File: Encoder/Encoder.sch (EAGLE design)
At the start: 4 parts, among them IC1 4017D

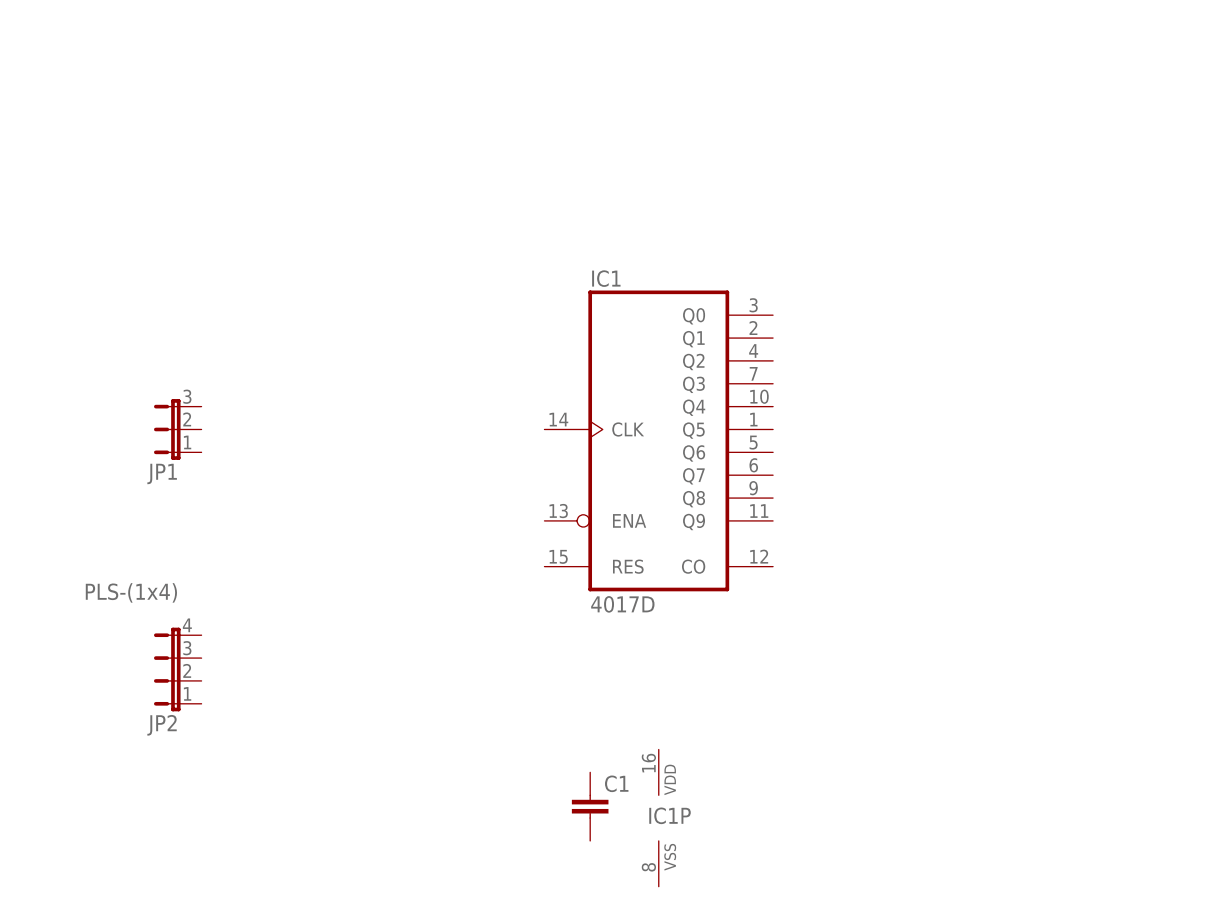
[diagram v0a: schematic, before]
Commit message: Added a pcb for encoder: made scheme, library and prearranged components on the board
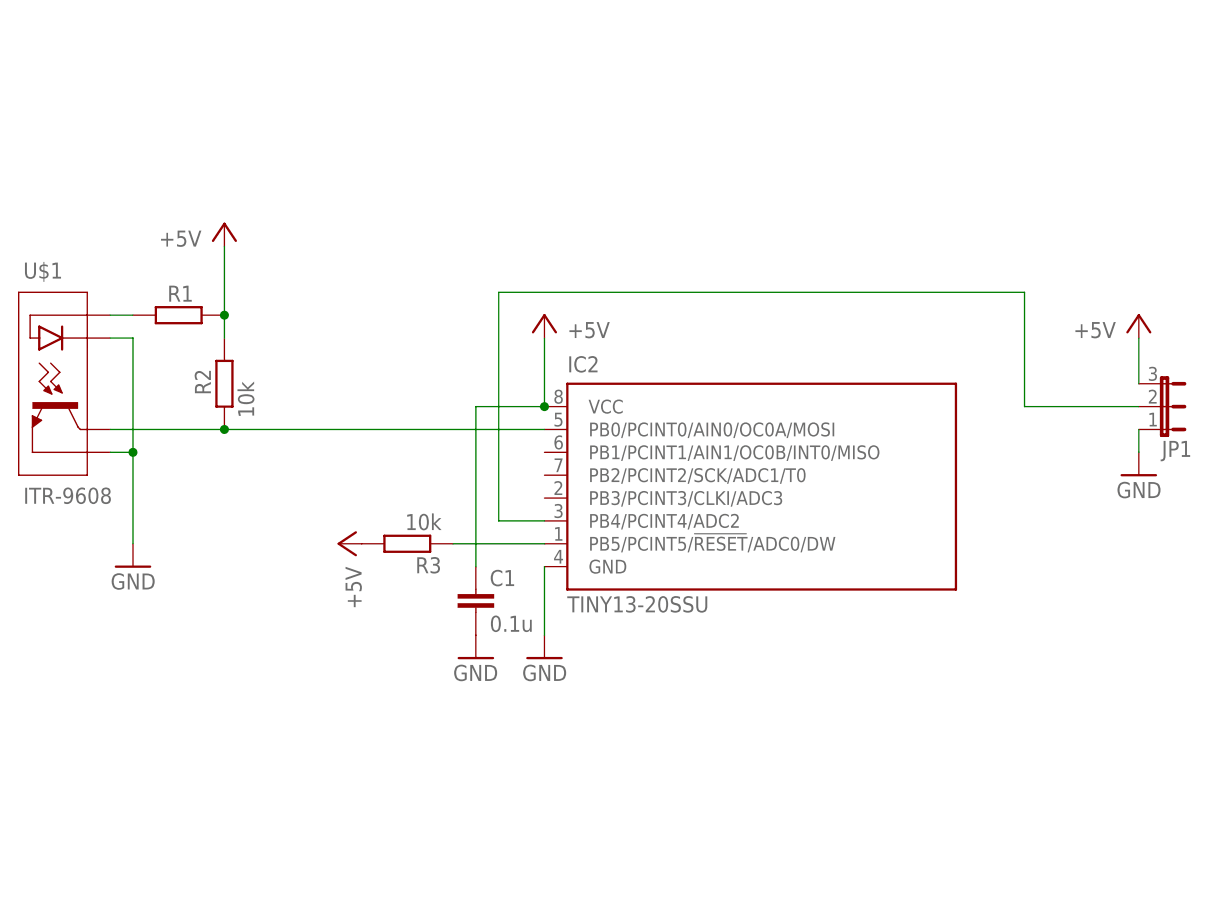
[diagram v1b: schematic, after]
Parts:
- removed IC1: 4017D, 40xx:4017D
- removed JP2: PLS-(1х4), jumper:PLS-(1х4)
- added IC2: TINY13-20SSU, atmel:TINY13-20SSU
- added R1: (no value), rcl:R-EU_M0805
- added R2, R3: 10k, rcl:R-EU_M0805
- added U$1: ITR-9608, EncoderLib:ITR-9608
- C1: value (none) -> 0.1u
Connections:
- new net !RES: IC2.PB5/PCINT5/!RESET!/ADC0/DW, R3.1
- new net +5V: C1.1, IC2.VCC, JP1.3, R1.2, R2.2, R3.2
- new net DATA-IN: IC2.PB0/PCINT0/AIN0/OC0A/MOSI, R2.1, U$1.C
- new net DATA-OUT: IC2.PB4/PCINT4/ADC2, JP1.2
- new net GND: C1.2, IC2.GND, JP1.1, U$1.E, U$1.K
- new net N$2: R1.1, U$1.A
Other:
- moved on the sheet: C1, JP1
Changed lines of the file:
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@@
 </classes>
 <parts>
-<part name="IC1" library="40xx" library_urn="urn:adsk.eagle:library:80" deviceset="4017" device="D" package3d_urn="urn:adsk.eagle:package:821/2"/>
-<part name="C1" library="rcl" library_urn="urn:adsk.eagle:library:334" deviceset="C-EU" device="C0805" package3d_urn="urn:adsk.eagle:package:23617/2"/>
+<part name="C1" library="rcl" library_urn="urn:adsk.eagle:library:334" deviceset="C-EU" device="C0805" package3d_urn="urn:adsk.eagle:package:23617/2" value="0.1u"/>
 <part name="JP1" library="jumper" library_urn="urn:adsk.eagle:library:252" deviceset="JP2E" device="" package3d_urn="urn:adsk.eagle:package:15452/1"/>
-<part name="JP2" library="jumper" deviceset="PLS-(1х4)" device=""/>
+<part name="R1" library="rcl" library_urn="urn:adsk.eagle:library:334" deviceset="R-EU_" device="M0805" package3d_urn="urn:adsk.eagle:package:23556/2"/>
+<part name="P+1" library="supply1" library_urn="urn:adsk.eagle:library:371" deviceset="+5V" device=""/>
+<part name="GND1" library="supply1" library_urn="urn:adsk.eagle:library:371" deviceset="GND" device=""/>
+<part name="P+2" library="supply1" library_urn="urn:adsk.eagle:library:371" deviceset="+5V" device=""/>
+<part name="GND2" library="supply1" library_urn="urn:adsk.eagle:library:371" deviceset="GND" device=""/>
+<part name="P+3" library="supply1" library_urn="urn:adsk.eagle:library:371" deviceset="+5V" device=""/>
+<part name="GND3" library="supply1" library_urn="urn:adsk.eagle:library:371" deviceset="GND" device=""/>
+<part name="R2" library="rcl" library_urn="urn:adsk.eagle:library:334" deviceset="R-EU_" device="M0805" package3d_urn="urn:adsk.eagle:package:23556/2" value="10k"/>
+<part name="IC2" library="atmel" library_urn="urn:adsk.eagle:library:105" deviceset="TINY13" device="SSU" package3d_urn="urn:adsk.eagle:package:4358/1" technology="-20"/>
+<part name="R3" library="rcl" library_urn="urn:adsk.eagle:library:334" deviceset="R-EU_" device="M0805" package3d_urn="urn:adsk.eagle:package:23556/2" value="10k"/>
+<part name="GND4" library="supply1" library_urn="urn:adsk.eagle:library:371" deviceset="GND" device=""/>
+<part name="P+4" library="supply1" library_urn="urn:adsk.eagle:library:371" deviceset="+5V" device=""/>
+<part name="U$1" library="EncoderLib" deviceset="ITR-9608" device=""/>
 </parts>
 <sheets>
@@
 </plain>
 <instances>
-<instance part="IC1" gate="A" x="53.34" y="55.88" smashed="yes">
-<attribute name="NAME" x="45.72" y="71.755" size="1.778" layer="95"/>
-<attribute name="VALUE" x="45.72" y="35.56" size="1.778" layer="96"/>
+<instance part="C1" gate="G$1" x="33.02" y="38.1" smashed="yes">
+<attribute name="NAME" x="34.544" y="38.481" size="1.778" layer="95"/>
+<attribute name="VALUE" x="34.544" y="33.401" size="1.778" layer="96"/>
 </instance>
-<instance part="IC1" gate="P" x="53.34" y="12.7" smashed="yes">
-<attribute name="NAME" x="52.07" y="12.065" size="1.778" layer="95"/>
+<instance part="JP1" gate="1" x="109.22" y="58.42" smashed="yes" rot="MR90">
+<attribute name="NAME" x="109.22" y="54.61" size="1.778" layer="95" rot="MR180"/>
+<attribute name="VALUE" x="109.22" y="64.135" size="1.778" layer="96" rot="MR180"/>
 </instance>
-<instance part="C1" gate="G$1" x="45.72" y="15.24" smashed="yes">
-<attribute name="NAME" x="47.244" y="15.621" size="1.778" layer="95"/>
-<attribute name="VALUE" x="47.244" y="10.541" size="1.778" layer="96"/>
+<instance part="R1" gate="G$1" x="0" y="68.58" smashed="yes">
+<attribute name="NAME" x="-1.27" y="70.0786" size="1.778" layer="95"/>
+<attribute name="VALUE" x="-3.81" y="65.278" size="1.778" layer="96"/>
 </instance>
-<instance part="JP1" gate="1" x="0" y="55.88" smashed="yes" rot="R90">
-<attribute name="NAME" x="0" y="52.07" size="1.778" layer="95" rot="R180"/>
-<attribute name="VALUE" x="0" y="61.595" size="1.778" layer="96" rot="R180"/>
+<instance part="P+1" gate="1" x="40.64" y="68.58" smashed="yes">
+<attribute name="VALUE" x="43.18" y="66.04" size="1.778" layer="96"/>
 </instance>
-<instance part="JP2" gate="G$1" x="0" y="30.48" smashed="yes" rot="R90">
-<attribute name="NAME" x="0" y="24.13" size="1.778" layer="95" rot="R180"/>
-<attribute name="VALUE" x="0" y="38.735" size="1.778" layer="96" rot="R180"/>
+<instance part="GND1" gate="1" x="33.02" y="30.48" smashed="yes">
+<attribute name="VALUE" x="30.48" y="27.94" size="1.778" layer="96"/>
+</instance>
+<instance part="P+2" gate="1" x="106.68" y="68.58" smashed="yes" rot="MR0">
+<attribute name="VALUE" x="104.14" y="66.04" size="1.778" layer="96" rot="MR0"/>
+</instance>
+<instance part="GND2" gate="1" x="106.68" y="50.8" smashed="yes" rot="MR0">
+<attribute name="VALUE" x="109.22" y="48.26" size="1.778" layer="96" rot="MR0"/>
+</instance>
+<instance part="P+3" gate="1" x="5.08" y="78.74" smashed="yes" rot="MR0">
+<attribute name="VALUE" x="2.54" y="76.2" size="1.778" layer="96" rot="MR0"/>
+</instance>
+<instance part="GND3" gate="1" x="-5.08" y="40.64" smashed="yes" rot="MR0">
+<attribute name="VALUE" x="-2.54" y="38.1" size="1.778" layer="96" rot="MR0"/>
+</instance>
+<instance part="R2" gate="G$1" x="5.08" y="60.96" smashed="yes" rot="R90">
+<attribute name="NAME" x="3.5814" y="59.69" size="1.778" layer="95" rot="R90"/>
+<attribute name="VALUE" x="8.382" y="57.15" size="1.778" layer="96" rot="R90"/>
+</instance>
+<instance part="IC2" gate="G$1" x="60.96" y="45.72" smashed="yes">
+<attribute name="NAME" x="43.18" y="62.23" size="1.778" layer="95"/>
+<attribute name="VALUE" x="43.18" y="35.56" size="1.778" layer="96"/>
+</instance>
+<instance part="R3" gate="G$1" x="25.4" y="43.18" smashed="yes" rot="R180">
+<attribute name="NAME" x="29.21" y="41.6814" size="1.778" layer="95" rot="R180"/>
+<attribute name="VALUE" x="29.21" y="46.482" size="1.778" layer="96" rot="R180"/>
+</instance>
+<instance part="GND4" gate="1" x="40.64" y="30.48" smashed="yes" rot="MR0">
+<attribute name="VALUE" x="43.18" y="27.94" size="1.778" layer="96" rot="MR0"/>
+</instance>
+<instance part="P+4" gate="1" x="17.78" y="43.18" smashed="yes" rot="MR270">
+<attribute name="VALUE" x="20.32" y="40.64" size="1.778" layer="96" rot="MR270"/>
+</instance>
+<instance part="U$1" gate="G$1" x="-12.7" y="60.96" smashed="yes">
+<attribute name="NAME" x="-17.272" y="72.644" size="1.778" layer="95"/>
+<attribute name="VALUE" x="-17.272" y="47.625" size="1.778" layer="96"/>
 </instance>
 </instances>
@@
 </busses>
 <nets>
+<net name="+5V" class="0">
+<segment>
+<pinref part="JP1" gate="1" pin="3"/>
+<pinref part="P+2" gate="1" pin="+5V"/>
+<wire x1="106.68" y1="60.96" x2="106.68" y2="66.04" width="0.1524" layer="91"/>
+</segment>
+<segment>
+<pinref part="P+3" gate="1" pin="+5V"/>
+<pinref part="R1" gate="G$1" pin="2"/>
+<wire x1="5.08" y1="76.2" x2="5.08" y2="68.58" width="0.1524" layer="91"/>
+<pinref part="R2" gate="G$1" pin="2"/>
+<wire x1="5.08" y1="66.04" x2="5.08" y2="68.58" width="0.1524" layer="91"/>
+<junction x="5.08" y="68.58"/>
+</segment>
+<segment>
+<pinref part="R3" gate="G$1" pin="2"/>
+<pinref part="P+4" gate="1" pin="+5V"/>
+</segment>
+<segment>
+<pinref part="IC2" gate="G$1" pin="VCC"/>
+<pinref part="P+1" gate="1" pin="+5V"/>
+<wire x1="40.64" y1="58.42" x2="40.64" y2="66.04" width="0.1524" layer="91"/>
+<pinref part="C1" gate="G$1" pin="1"/>
+<wire x1="33.02" y1="40.64" x2="33.02" y2="58.42" width="0.1524" layer="91"/>
+<wire x1="33.02" y1="58.42" x2="40.64" y2="58.42" width="0.1524" layer="91"/>
+<junction x="40.64" y="58.42"/>
+</segment>
+</net>
+<net name="GND" class="0">
+<segment>
+<pinref part="JP1" gate="1" pin="1"/>
+<pinref part="GND2" gate="1" pin="GND"/>
+<wire x1="106.68" y1="55.88" x2="106.68" y2="53.34" width="0.1524" layer="91"/>
+</segment>
+<segment>
+<pinref part="GND3" gate="1" pin="GND"/>
+<wire x1="-7.62" y1="66.04" x2="-5.08" y2="66.04" width="0.1524" layer="91"/>
+<wire x1="-5.08" y1="66.04" x2="-5.08" y2="53.34" width="0.1524" layer="91"/>
+<wire x1="-5.08" y1="53.34" x2="-5.08" y2="43.18" width="0.1524" layer="91"/>
+<wire x1="-7.62" y1="53.34" x2="-5.08" y2="53.34" width="0.1524" layer="91"/>
+<junction x="-5.08" y="53.34"/>
+<pinref part="U$1" gate="G$1" pin="K"/>
+<pinref part="U$1" gate="G$1" pin="E"/>
+</segment>
+<segment>
+<pinref part="IC2" gate="G$1" pin="GND"/>
+<pinref part="GND4" gate="1" pin="GND"/>
+<wire x1="40.64" y1="33.02" x2="40.64" y2="40.64" width="0.1524" layer="91"/>
+</segment>
+<segment>
+<pinref part="C1" gate="G$1" pin="2"/>
+<pinref part="GND1" gate="1" pin="GND"/>
+</segment>
+</net>
+<net name="N$2" class="0">
+<segment>
+<pinref part="R1" gate="G$1" pin="1"/>
+<wire x1="-5.08" y1="68.58" x2="-7.62" y2="68.58" width="0.1524" layer="91"/>
+<pinref part="U$1" gate="G$1" pin="A"/>
+</segment>
+</net>
+<net name="DATA-IN" class="0">
+<segment>
+<pinref part="R2" gate="G$1" pin="1"/>
+<wire x1="5.08" y1="55.88" x2="-7.62" y2="55.88" width="0.1524" layer="91"/>
+<pinref part="U$1" gate="G$1" pin="C"/>
+<pinref part="IC2" gate="G$1" pin="PB0/PCINT0/AIN0/OC0A/MOSI"/>
+<wire x1="5.08" y1="55.88" x2="40.64" y2="55.88" width="0.1524" layer="91"/>
+<junction x="5.08" y="55.88"/>
+</segment>
+</net>
+<net name="!RES" class="0">
+<segment>
+<pinref part="R3" gate="G$1" pin="1"/>
+<pinref part="IC2" gate="G$1" pin="PB5/PCINT5/!RESET!/ADC0/DW"/>
+<wire x1="30.48" y1="43.18" x2="40.64" y2="43.18" width="0.1524" layer="91"/>
+</segment>
+</net>
+<net name="DATA-OUT" class="0">
+<segment>
+<pinref part="IC2" gate="G$1" pin="PB4/PCINT4/ADC2"/>
+<wire x1="40.64" y1="45.72" x2="35.56" y2="45.72" width="0.1524" layer="91"/>
+<wire x1="35.56" y1="45.72" x2="35.56" y2="71.12" width="0.1524" layer="91"/>
+<wire x1="35.56" y1="71.12" x2="93.98" y2="71.12" width="0.1524" layer="91"/>
+<wire x1="93.98" y1="71.12" x2="93.98" y2="58.42" width="0.1524" layer="91"/>
+<pinref part="JP1" gate="1" pin="2"/>
+<wire x1="93.98" y1="58.42" x2="106.68" y2="58.42" width="0.1524" layer="91"/>
+</segment>
+</net>
 </nets>
 </sheet>

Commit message: Added connector for programmer. Increased the place for the encoder.
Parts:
- added JP2: ISP, jumper:JP3Q
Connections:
- new net N$1: IC2.PB1/PCINT1/AIN1/OC0B/INT0/MISO, JP2.1
- new net N$3: IC2.PB2/PCINT2/SCK/ADC1/T0, JP2.3
- net !RES: now also JP2.5
- net +5V: now also JP2.2
- net DATA-IN: now also JP2.4
- net GND: now also JP2.6
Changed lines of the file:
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@@
 <part name="P+4" library="supply1" library_urn="urn:adsk.eagle:library:371" deviceset="+5V" device=""/>
 <part name="U$1" library="EncoderLib" deviceset="ITR-9608" device=""/>
+<part name="JP2" library="jumper" library_urn="urn:adsk.eagle:library:252" deviceset="JP3Q" device="" package3d_urn="urn:adsk.eagle:package:15460/1" value="ISP"/>
+<part name="P+5" library="supply1" library_urn="urn:adsk.eagle:library:371" deviceset="+5V" device=""/>
+<part name="GND5" library="supply1" library_urn="urn:adsk.eagle:library:371" deviceset="GND" device=""/>
 </parts>
 <sheets>
@@
 <attribute name="VALUE" x="-17.272" y="47.625" size="1.778" layer="96"/>
 </instance>
+<instance part="JP2" gate="B" x="27.94" y="88.9" smashed="yes">
+<attribute name="NAME" x="22.86" y="83.82" size="1.778" layer="95" rot="R90"/>
+<attribute name="VALUE" x="34.925" y="83.82" size="1.778" layer="96" rot="R90"/>
+</instance>
+<instance part="P+5" gate="1" x="17.78" y="96.52" smashed="yes" rot="MR270">
+<attribute name="VALUE" x="20.32" y="93.98" size="1.778" layer="96" rot="MR270"/>
+</instance>
+<instance part="GND5" gate="1" x="35.56" y="96.52" smashed="yes" rot="MR270">
+<attribute name="VALUE" x="38.1" y="99.06" size="1.778" layer="96" rot="MR270"/>
+</instance>
 </instances>
 <busses>
@@
 <wire x1="33.02" y1="58.42" x2="40.64" y2="58.42" width="0.1524" layer="91"/>
 <junction x="40.64" y="58.42"/>
+</segment>
+<segment>
+<pinref part="P+5" gate="1" pin="+5V"/>
+<pinref part="JP2" gate="B" pin="2"/>
+<wire x1="20.32" y1="96.52" x2="25.4" y2="96.52" width="0.1524" layer="91"/>
 </segment>
 </net>
@@
 <pinref part="GND1" gate="1" pin="GND"/>
 </segment>
+<segment>
+<pinref part="JP2" gate="B" pin="6"/>
+<pinref part="GND5" gate="1" pin="GND"/>
+<wire x1="30.48" y1="96.52" x2="33.02" y2="96.52" width="0.1524" layer="91"/>
+</segment>
 </net>
 <net name="N$2" class="0">
@@
 <pinref part="U$1" gate="G$1" pin="C"/>
 <pinref part="IC2" gate="G$1" pin="PB0/PCINT0/AIN0/OC0A/MOSI"/>
-<wire x1="5.08" y1="55.88" x2="40.64" y2="55.88" width="0.1524" layer="91"/>
+<wire x1="5.08" y1="55.88" x2="15.24" y2="55.88" width="0.1524" layer="91"/>
 <junction x="5.08" y="55.88"/>
+<pinref part="JP2" gate="B" pin="4"/>
+<wire x1="15.24" y1="55.88" x2="40.64" y2="55.88" width="0.1524" layer="91"/>
+<wire x1="27.94" y1="96.52" x2="27.94" y2="101.6" width="0.1524" layer="91"/>
+<wire x1="27.94" y1="101.6" x2="15.24" y2="101.6" width="0.1524" layer="91"/>
+<wire x1="15.24" y1="101.6" x2="15.24" y2="55.88" width="0.1524" layer="91"/>
+<junction x="15.24" y="55.88"/>
 </segment>
 </net>
@@
 <pinref part="IC2" gate="G$1" pin="PB5/PCINT5/!RESET!/ADC0/DW"/>
 <wire x1="30.48" y1="43.18" x2="40.64" y2="43.18" width="0.1524" layer="91"/>
+<pinref part="JP2" gate="B" pin="5"/>
+<wire x1="30.48" y1="81.28" x2="30.48" y2="43.18" width="0.1524" layer="91"/>
+<junction x="30.48" y="43.18"/>
 </segment>
 </net>
@@
 </segment>
 </net>
+<net name="N$1" class="0">
+<segment>
+<pinref part="JP2" gate="B" pin="1"/>
+<pinref part="IC2" gate="G$1" pin="PB1/PCINT1/AIN1/OC0B/INT0/MISO"/>
+<wire x1="25.4" y1="81.28" x2="25.4" y2="53.34" width="0.1524" layer="91"/>
+<wire x1="25.4" y1="53.34" x2="40.64" y2="53.34" width="0.1524" layer="91"/>
+</segment>
+</net>
+<net name="N$3" class="0">
+<segment>
+<pinref part="JP2" gate="B" pin="3"/>
+<pinref part="IC2" gate="G$1" pin="PB2/PCINT2/SCK/ADC1/T0"/>
+<wire x1="27.94" y1="81.28" x2="27.94" y2="50.8" width="0.1524" layer="91"/>
+<wire x1="27.94" y1="50.8" x2="40.64" y2="50.8" width="0.1524" layer="91"/>
+</segment>
+</net>
